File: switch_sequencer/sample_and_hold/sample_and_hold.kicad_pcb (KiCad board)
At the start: 2 copper layers, 35.3 x 128.5 mm, 38 parts, among them J12 Eurorack_Power_10pin_Shrouded, J14 3.5mm_Mono_Switched_sm, J15 3.5mm_Mono_Switched_sm, J16 3.5mm_Mono_Switched_sm, J17 3.5mm_Mono_Switched_sm, J18 3.5mm_Mono_Switched_sm, J19 3.5mm_Mono_Switched_sm, U1 TL072, U2 LF398_SOIC8, U3 TL072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

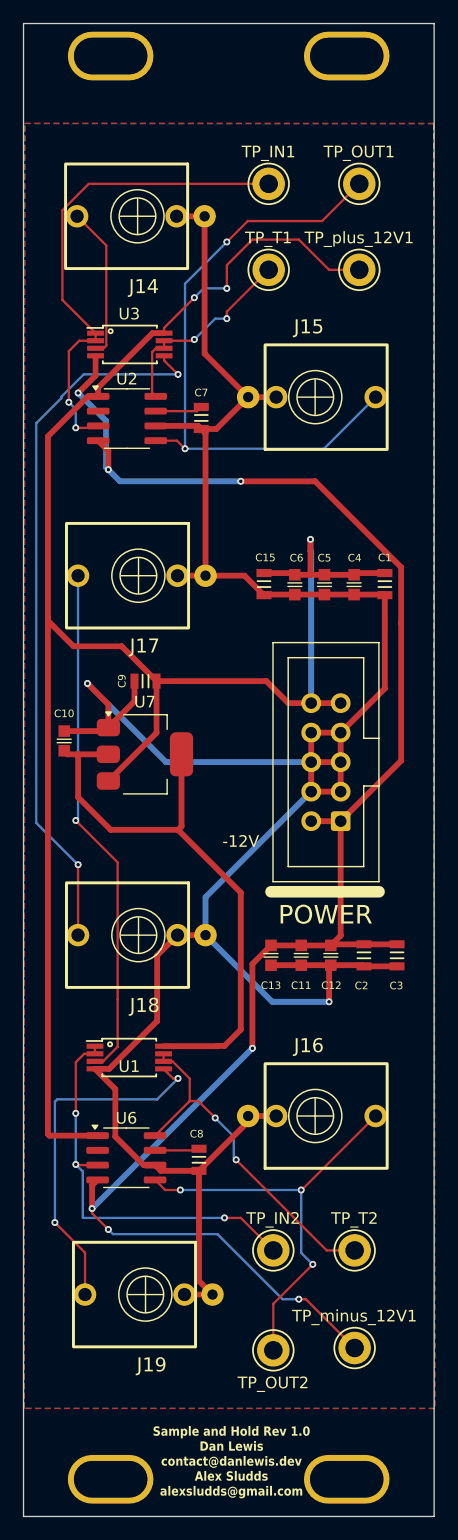
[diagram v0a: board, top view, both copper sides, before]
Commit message: finish attenuverters, sample and hold
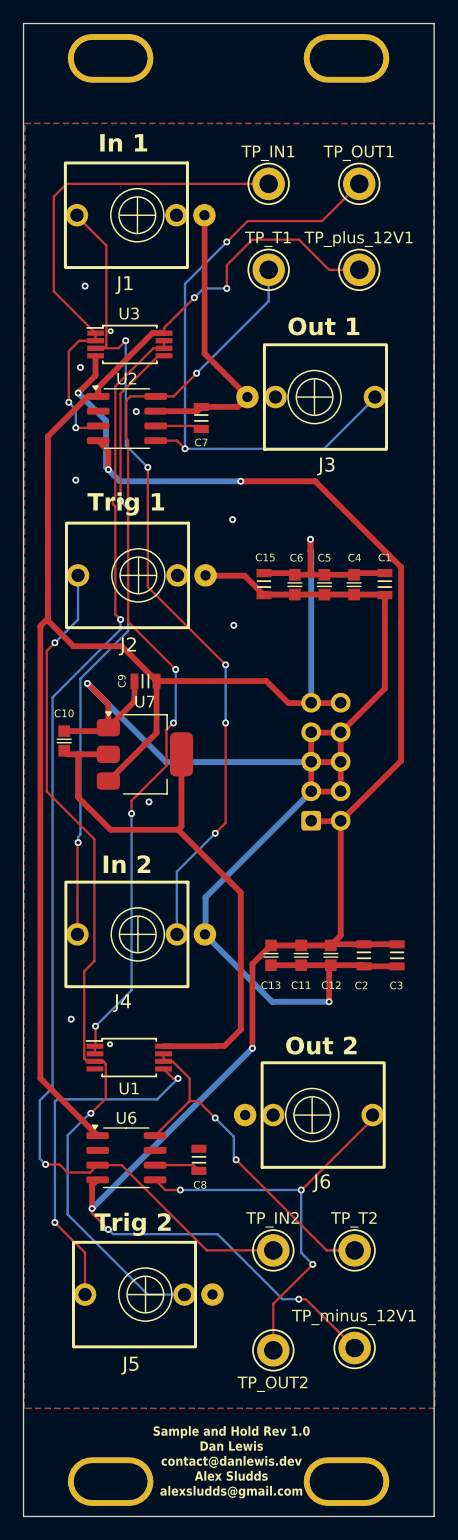
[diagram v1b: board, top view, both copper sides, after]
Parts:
- removed J12: Eurorack_Power_10pin_Shrouded, 4ms_Connector:Pins_2x05_2.54mm_TH_EurorackPower_Shrouded
- removed J14, J15, J16, J17, J18, J19: 3.5mm_Mono_Switched_sm, 4ms_Jack:EighthInch_PJ398SM
- added J1: 3.5mm_Mono_Switched_sm, 4ms_Jack:EighthInch_PJ398SM, F.Cu at (68.7, 30.7)
- added J2: 3.5mm_Mono_Switched_sm, 4ms_Jack:EighthInch_PJ398SM, F.Cu at (68.8, 61.7)
- added J3: 3.5mm_Mono_Switched_sm, 4ms_Jack:EighthInch_PJ398SM, F.Cu at (83.9, 46.4)
- added J4: 3.5mm_Mono_Switched_sm, 4ms_Jack:EighthInch_PJ398SM, F.Cu at (68.7, 92.6)
- added J5: 3.5mm_Mono_Switched_sm, 4ms_Jack:EighthInch_PJ398SM, F.Cu at (69.4, 123.6)
- added J6: 3.5mm_Mono_Switched_sm, 4ms_Jack:EighthInch_PJ398SM, F.Cu at (83.7, 108.2)
- added J7: Eurorack_Power_10pin_Shrouded, 4ms_Connector:Pins_2x05_2.54mm_TH_EurorackPower_Shrouded, B.Cu at (84.9, 77.7)
- moved H3 0.20 mm to (86.8, 139.4)
- moved H1 0.20 mm to (97.2, 18.0)
- moved H2 0.20 mm to (66.6, 20.2)
- moved H4 0.20 mm to (67.4, 144.0)
- turned C7 to 90 degrees
- turned C8 to 90 degrees
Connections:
- C7 pad 1: /T1 -> Net-(U2-C_{h})
- C8 pad 1: /T2 -> Net-(U6-C_{h})
- TP_IN2 pad 1: Net-(U1A--) -> Net-(U3B--)
- TP_T1 pad 1: Net-(U2-Hold) -> Net-(U1A--)
- U1 pad 3: Net-(J17-SIG) -> TRIG 1
- U2 pad 6: GND -> Net-(U2-C_{h})
- U2 pad 7: /T1 -> GND
- U2 pad 8: Net-(U2-Hold) -> Net-(U1A--)
- U3 pad 3: Net-(J14-SIG) -> SIGNAL 1
- U3 pad 6: Net-(U2-Hold) -> Net-(U3B--)
- U3 pad 7: Net-(U2-Hold) -> Net-(U3B--)
- U6 pad 3: Net-(U1A--) -> Net-(U3B--)
- U6 pad 6: GND -> Net-(U6-C_{h})
- U6 pad 7: /T2 -> GND
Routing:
- net Net-(U3B--): track 0.00 -> 99.8 mm, vias 0 -> 2
- net GND: track 227.4 -> 152.3 mm, vias 2 -> 10
- net TRIG 1: track 0.00 -> 74.1 mm, vias 0 -> 2
- net SIGNAL 1: track 0.00 -> 72.5 mm, vias 0 -> 5
- net Net-(J17-SIG): track 44.6 -> 0.00 mm, vias 1 -> 0
- net Net-(U1A--): track 35.7 -> 79.4 mm, vias 3 -> 5
- net Net-(U2-Hold): track 17.6 -> 0.00 mm, vias 2 -> 0
- net Net-(J14-SIG): track 13.2 -> 0.00 mm
- net Net-(J4-SIG): track 61.7 -> 53.7 mm
- net /T1: track 4.08 -> 0.00 mm
- net Net-(U2-C_{h}): track 0.00 -> 4.03 mm
- net Net-(U6-C_{h}): track 0.00 -> 3.98 mm
- net /T2: track 3.83 -> 0.00 mm
- net +12V: track 167.5 -> 165.6 mm
- net Net-(U2-I): track 42.6 -> 44.4 mm
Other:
- board text added: "In 1"
- board text added: "In 2"
- board text added: "Out 1"
- board text added: "Out 2"
- board text added: "Trig 1"
- board text added: "Trig 2"
